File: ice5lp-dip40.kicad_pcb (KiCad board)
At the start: 2 copper layers, 17.8 x 50.8 mm, 43 parts, among them J1 Conn_02x04_Odd_Even, J2 Conn_01x20, J3 Conn_01x20, J4 USB_B_Micro, SW1 SW_Push, SW2 SW_Push, U1 AT25D011-SSHF, U2 MIC5355-S4YMME, U3 ICE5LP4K-SG48, X1 ECS-2520MV-500-BN-TR

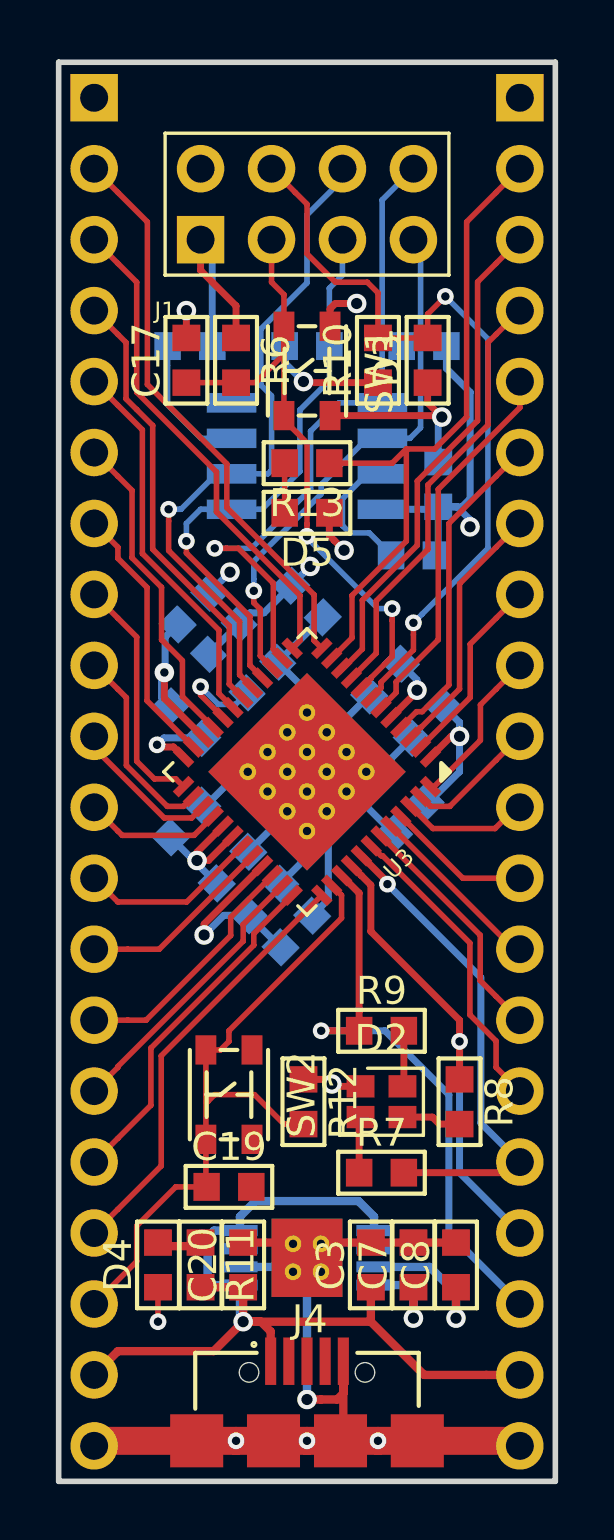
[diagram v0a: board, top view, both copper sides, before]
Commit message: Fix some DRC errors on PCB
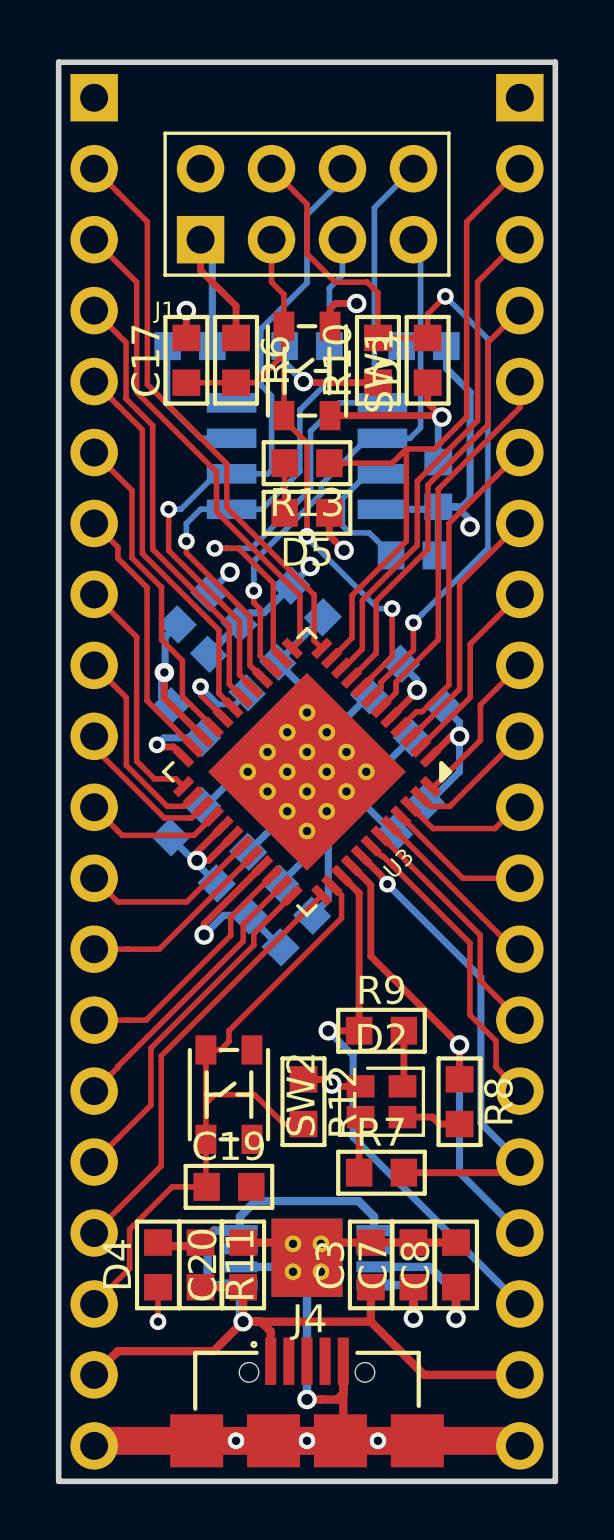
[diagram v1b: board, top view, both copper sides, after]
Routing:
- net RGB_B: track 21.3 -> 19.6 mm
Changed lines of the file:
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@@
   (segment (start 191.262 73.66) (end 191.262 74.295) (width 0.2) (layer B.Cu) (net 6))
   (segment (start 191.77 73.152) (end 191.262 73.66) (width 0.2) (layer B.Cu) (net 6))
-  (segment (start 198.269999 68.781999) (end 198.269999 62.080001) (width 0.2) (layer B.Cu) (net 7))
-  (segment (start 198.28 69.342) (end 198.28 68.792) (width 0.2) (layer B.Cu) (net 7) (status 10))
-  (segment (start 198.269999 62.080001) (end 199.39 60.96) (width 0.2) (layer B.Cu) (net 7) (status 20))
-  (segment (start 198.28 68.792) (end 198.269999 68.781999) (width 0.2) (layer B.Cu) (net 7))
   (via (at 192.278 74.549) (size 0.6) (drill 0.3) (layers F.Cu B.Cu) (net 7))
   (segment (start 195.707 70.358) (end 195.707 72.433264) (width 0.2) (layer B.Cu) (net 7))
@@
   (segment (start 194.372002 75.799398) (end 193.121602 74.549) (width 0.2) (layer F.Cu) (net 7))
   (segment (start 192.702264 74.549) (end 192.278 74.549) (width 0.2) (layer F.Cu) (net 7))
+  (segment (start 197.993 62.357) (end 199.39 60.96) (width 0.2) (layer B.Cu) (net 7))
+  (segment (start 197.993 68.505) (end 197.993 62.357) (width 0.2) (layer B.Cu) (net 7))
+  (segment (start 198.28 69.342) (end 198.28 68.792) (width 0.2) (layer B.Cu) (net 7))
+  (segment (start 198.28 68.792) (end 197.993 68.505) (width 0.2) (layer B.Cu) (net 7))
   (segment (start 190.589 68.01) (end 190.589 67.31) (width 0.2) (layer B.Cu) (net 8))
   (segment (start 190.589 69.411) (end 190.589 68.01) (width 0.2) (layer B.Cu) (net 8))
@@
   (segment (start 191.961 94.107) (end 191.961 94.361) (width 0.2) (layer F.Cu) (net 46))
   (segment (start 191.961 94.361) (end 191.961 95.707) (width 0.2) (layer F.Cu) (net 46) (status 20))
-  (segment (start 190.881 97.409) (end 191.986 97.409) (width 0.2) (layer F.Cu) (net 46) (status 20))
-  (segment (start 189.484 98.806) (end 190.881 97.409) (width 0.2) (layer F.Cu) (net 46))
-  (segment (start 187.96 101.6) (end 189.484 100.076) (width 0.2) (layer F.Cu) (net 46) (status 10))
-  (segment (start 189.484 100.076) (end 189.484 98.806) (width 0.2) (layer F.Cu) (net 46))
   (segment (start 193.699 94.107) (end 192.278 94.107) (width 0.2) (layer F.Cu) (net 46))
   (segment (start 195.453 95.161) (end 194.753 95.161) (width 0.2) (layer F.Cu) (net 46) (status 10))
@@
   (segment (start 191.961 92.507) (end 192.481 92.507) (width 0.2) (layer F.Cu) (net 46))
   (segment (start 192.481 92.507) (end 192.786 92.202) (width 0.2) (layer F.Cu) (net 46))
+  (segment (start 190.754 97.409) (end 191.986 97.409) (width 0.2) (layer F.Cu) (net 46))
+  (segment (start 189.23 98.933) (end 190.754 97.409) (width 0.2) (layer F.Cu) (net 46))
+  (segment (start 187.96 101.6) (end 189.23 100.33) (width 0.2) (layer F.Cu) (net 46))
+  (segment (start 189.23 100.33) (end 189.23 98.933) (width 0.2) (layer F.Cu) (net 46))
   (segment (start 197.447 91.121) (end 197.447 91.821) (width 0.25) (layer F.Cu) (net 47) (status 20))
   (segment (start 197.474009 91.093991) (end 197.447 91.121) (width 0.2) (layer F.Cu) (net 47))
-  (via (at 196.088 91.821) (size 0.6) (drill 0.3) (layers F.Cu B.Cu) (net 47))
-  (segment (start 197.447 91.821) (end 196.088 91.821) (width 0.25) (layer F.Cu) (net 47) (status 10))
-  (segment (start 200.66 94.107) (end 200.66 99.06) (width 0.25) (layer B.Cu) (net 47))
-  (segment (start 200.66 99.06) (end 203.2 101.6) (width 0.25) (layer B.Cu) (net 47) (status 20))
-  (segment (start 196.088 91.821) (end 198.374 91.821) (width 0.25) (layer B.Cu) (net 47))
-  (segment (start 198.374 91.821) (end 200.66 94.107) (width 0.25) (layer B.Cu) (net 47))
   (segment (start 196.817437 86.262311) (end 197.445989 86.890863) (width 0.25) (layer F.Cu) (net 47))
   (segment (start 197.445989 86.890863) (end 197.445989 91.065971) (width 0.25) (layer F.Cu) (net 47))
   (segment (start 197.445989 91.065971) (end 197.474009 91.093991) (width 0.25) (layer F.Cu) (net 47))
-  (segment (start 201.041 93.561) (end 201.041 92.202) (width 0.25) (layer F.Cu) (net 48) (status 10))
-  (via (at 201.041 92.202) (size 0.6) (drill 0.3) (layers F.Cu B.Cu) (net 48))
-  (segment (start 201.041 96.901) (end 203.2 99.06) (width 0.25) (layer B.Cu) (net 48) (status 20))
-  (segment (start 201.041 92.202) (end 201.041 96.901) (width 0.25) (layer B.Cu) (net 48))
-  (segment (start 197.524543 86.26231) (end 197.17099 85.908757) (width 0.25) (layer F.Cu) (net 48))
-  (segment (start 197.866 86.603767) (end 197.524543 86.26231) (width 0.25) (layer F.Cu) (net 48))
-  (segment (start 201.041 91.44) (end 197.866 88.265) (width 0.25) (layer F.Cu) (net 48))
-  (segment (start 197.866 88.265) (end 197.866 86.603767) (width 0.25) (layer F.Cu) (net 48))
-  (segment (start 201.041 92.202) (end 201.041 91.44) (width 0.25) (layer F.Cu) (net 48))
+  (via (at 196.342016 91.821) (size 0.7) (drill 0.4) (layers F.Cu B.Cu) (net 47))
+  (segment (start 197.447 91.821) (end 196.342016 91.821) (width 0.25) (layer F.Cu) (net 47))
+  (segment (start 203.2 101.6) (end 197.231 95.631) (width 0.25) (layer B.Cu) (net 47))
+  (segment (start 197.231 95.631) (end 197.231 92.709984) (width 0.25) (layer B.Cu) (net 47))
+  (segment (start 196.642015 92.120999) (end 196.342016 91.821) (width 0.25) (layer B.Cu) (net 47))
+  (segment (start 197.231 92.709984) (end 196.642015 92.120999) (width 0.25) (layer B.Cu) (net 47))
+  (via (at 201.041 92.32901) (size 0.7) (drill 0.4) (layers F.Cu B.Cu) (net 48))
+  (segment (start 201.041 93.561) (end 201.041 92.32901) (width 0.25) (layer F.Cu) (net 48))
+  (segment (start 200.691001 91.979011) (end 201.041 92.32901) (width 0.25) (layer F.Cu) (net 48))
+  (segment (start 201.041 96.901) (end 201.041 92.823984) (width 0.25) (layer B.Cu) (net 48))
+  (segment (start 201.041 92.823984) (end 201.041 92.32901) (width 0.25) (layer B.Cu) (net 48))
+  (segment (start 203.2 99.06) (end 201.041 96.901) (width 0.25) (layer B.Cu) (net 48))
+  (segment (start 197.866 89.15401) (end 200.691001 91.979011) (width 0.25) (layer F.Cu) (net 48))
+  (segment (start 197.866 86.603767) (end 197.866 89.15401) (width 0.25) (layer F.Cu) (net 48))
+  (segment (start 197.17099 85.908757) (end 197.866 86.603767) (width 0.25) (layer F.Cu) (net 48))
   (segment (start 202.819 96.901) (end 203.2 96.52) (width 0.2) (layer F.Cu) (net 49) (status 30))
   (segment (start 199.047 96.901) (end 202.819 96.901) (width 0.25) (layer F.Cu) (net 49) (status 30))

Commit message: Add 2 inner layers and route power
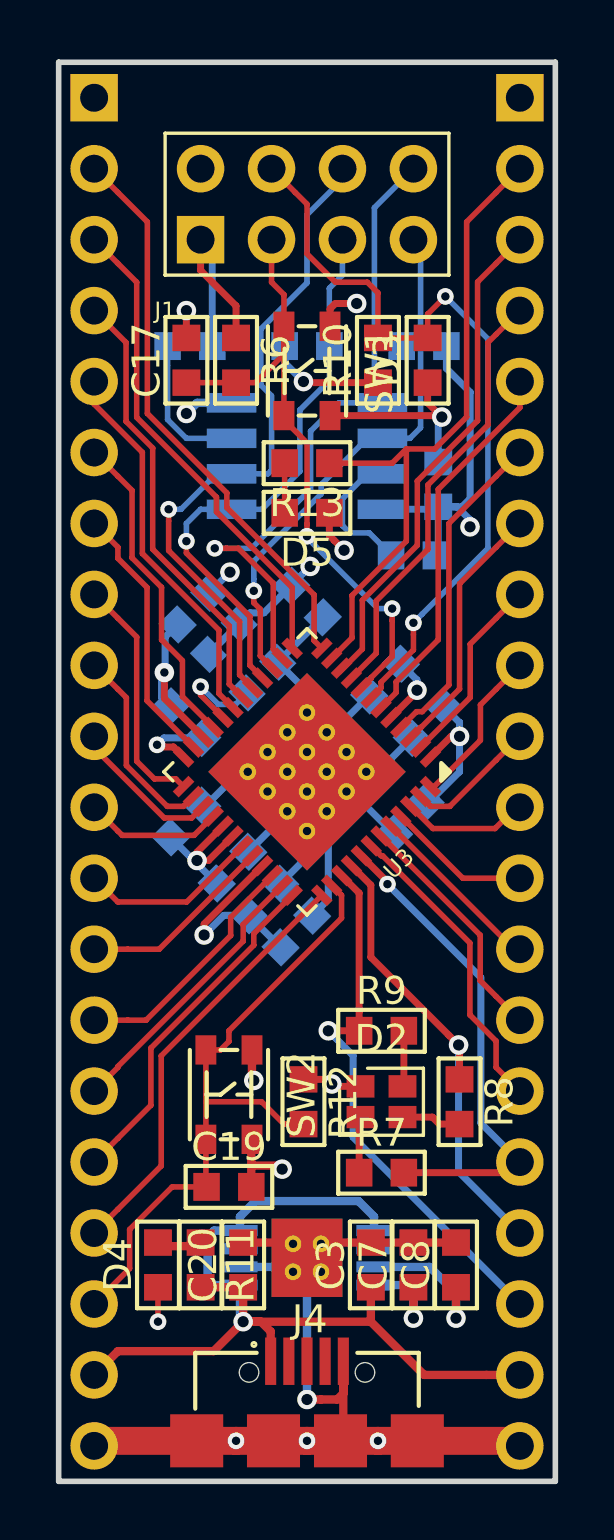
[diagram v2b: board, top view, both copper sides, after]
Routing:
- net VCC_IO: track 53.9 -> 177.6 mm
- net VCC_CORE: track 13.5 -> 46.8 mm
- net GND: track 83.7 -> 89.5 mm, vias 10 -> 13
- added copper zone on In2.GND.Cu, net GND
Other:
- copper layers 2 -> 4

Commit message: Increase power tracks width
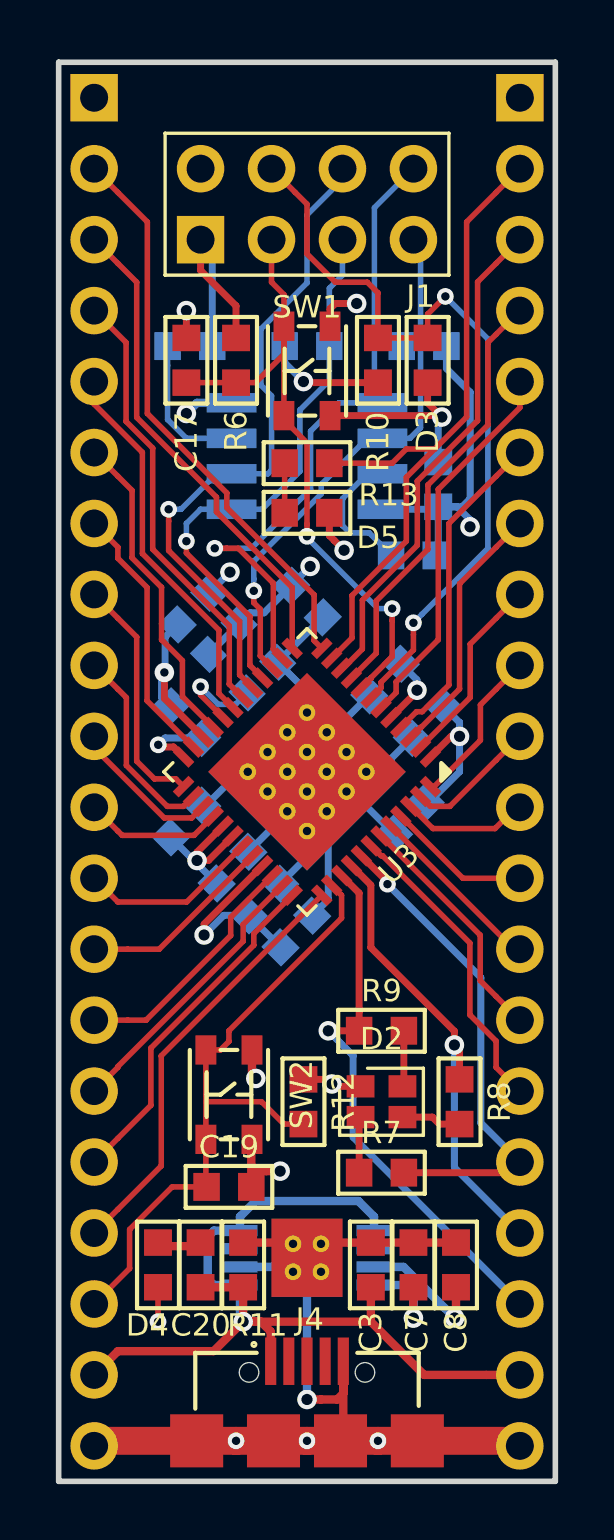
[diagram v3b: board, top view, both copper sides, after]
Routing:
- net VCC_IO: track 177.6 -> 178.8 mm
- net VCC_CORE: track 46.8 -> 46.2 mm

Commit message: Beautify Silk and Fab layers
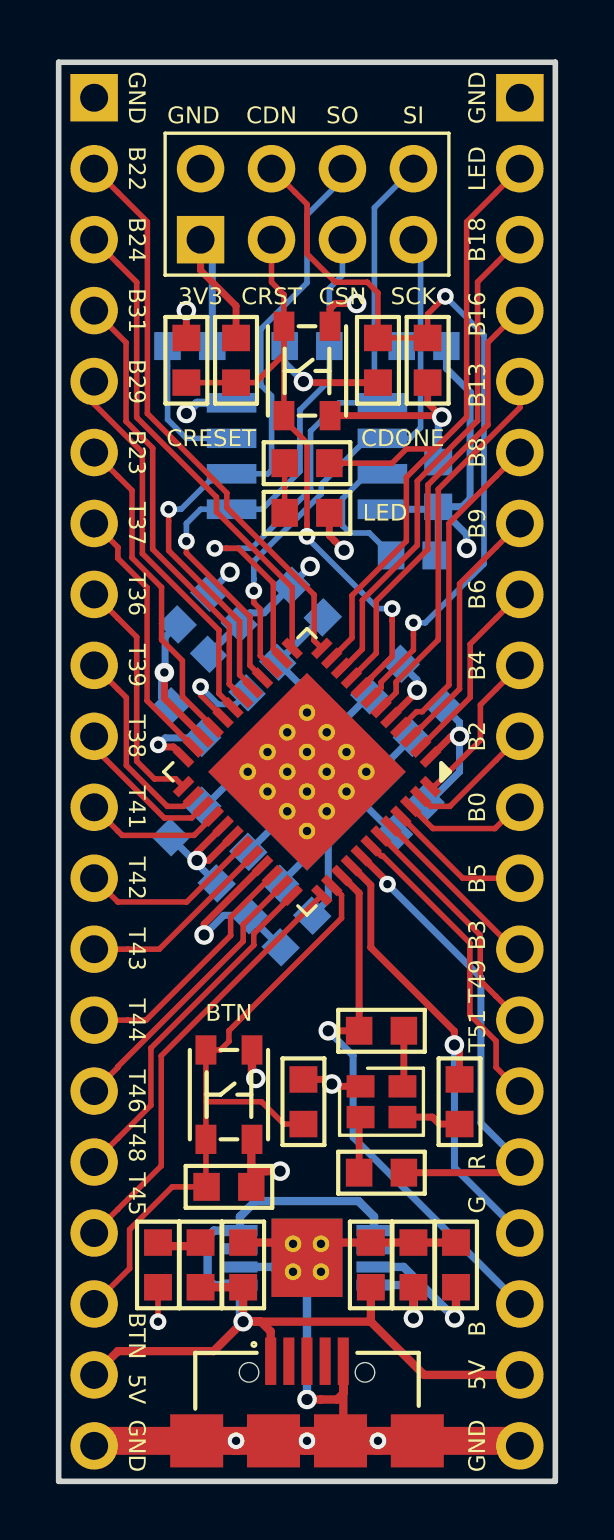
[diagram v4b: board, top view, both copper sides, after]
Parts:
- renumbered R2 to eR2
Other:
- board text added: "3V3"
- board text added: "5V"
- board text added: "B"
- board text added: "B0"
- board text added: "B13"
- board text added: "B16"
- board text added: "B18"
- board text added: "B2"
- board text added: "B22"
- board text added: "B23"
- board text added: "B24"
- board text added: "B29"
- board text added: "B3"
- board text added: "B31"
- board text added: "B4"
- board text added: "B5"
- board text added: "B6"
- board text added: "B8"
- board text added: "B9"
- board text added: "BTN"
- board text added: "CDN"
- board text added: "CDONE"
- board text added: "CRESET"
- board text added: "CRST"
- board text added: "CSN"
- board text added: "G"
- board text added: "GND"
- board text added: "LED"
- board text added: "R"
- board text added: "SCK"
- board text added: "SI"
- board text added: "SO"
- board text added: "T36"
- board text added: "T37"
- board text added: "T38"
- board text added: "T39"
- board text added: "T41"
- board text added: "T42"
- board text added: "T43"
- board text added: "T44"
- board text added: "T45"
- board text added: "T46"
- board text added: "T48"
- board text added: "T49"
- board text added: "T51"

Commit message: Add logo and final Silk edits
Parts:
- added G***: LOGO, esynr3z_Symbol:esynr3z_logo_4.5x8.4mm_Silk, B.Cu at (199.0, 93.2)
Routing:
- net IOT_42B: track 6.51 -> 5.80 mm
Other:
- board text added: "DIP40"
- board text added: "ICE5LP"
- board text added: "esynr3z"

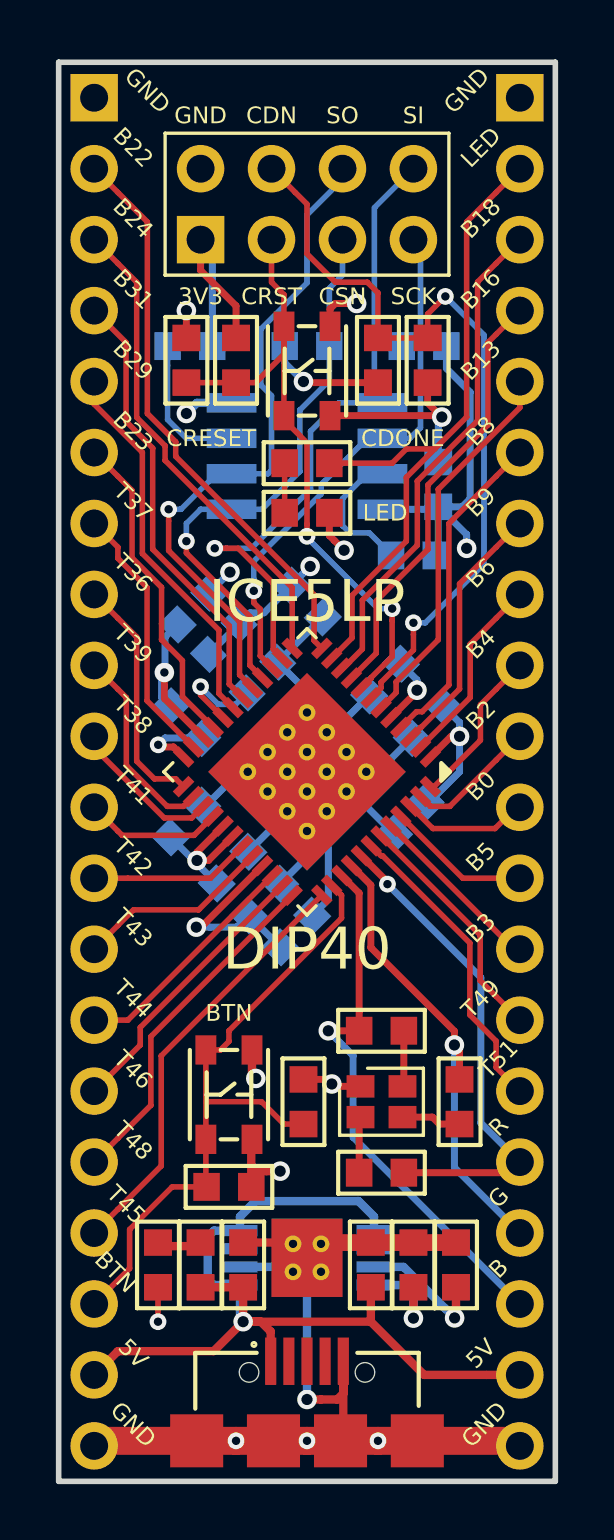
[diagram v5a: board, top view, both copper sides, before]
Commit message: Some minor pcb fixes
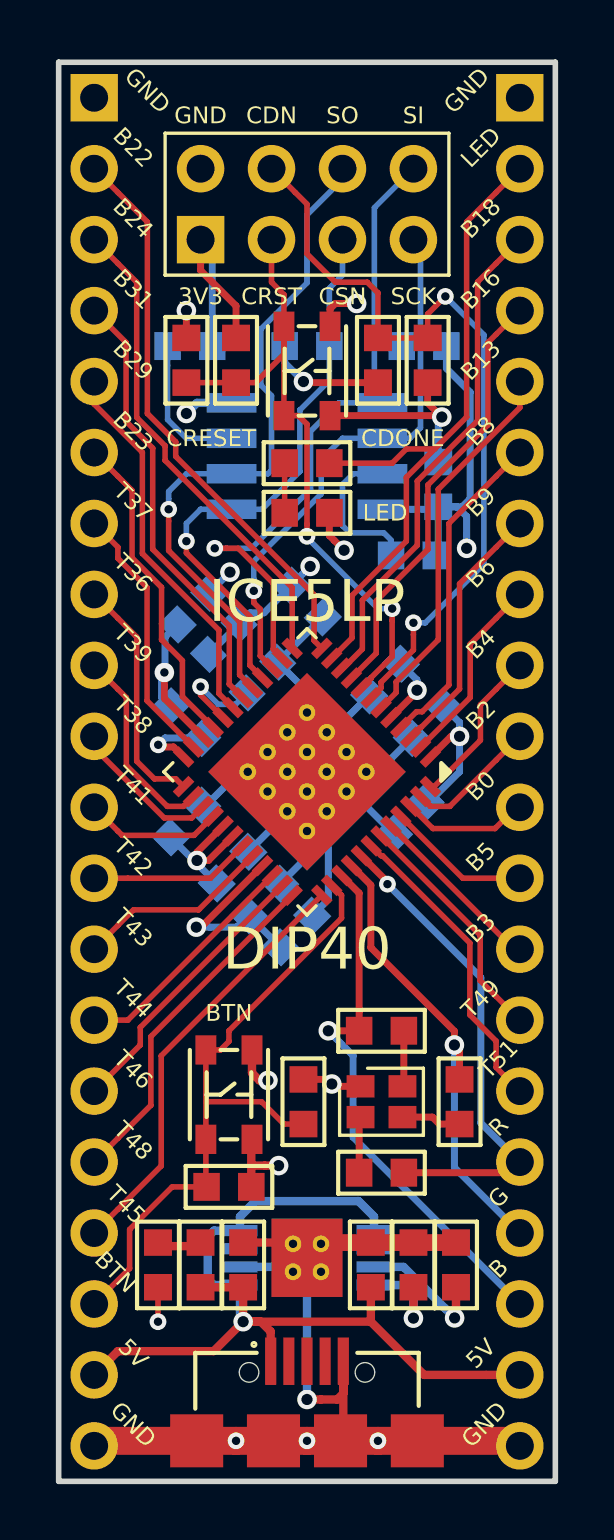
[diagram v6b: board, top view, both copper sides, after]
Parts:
- renumbered eR2 to R2
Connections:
- J4 pad 2: (no net) -> Net-(J4-Pad2)
- J4 pad 3: (no net) -> Net-(J4-Pad3)
- J4 pad 4: (no net) -> Net-(J4-Pad4)
- U2 pad 3: (no net) -> Net-(U2-Pad3)
- U2 pad 6: (no net) -> Net-(U2-Pad6)
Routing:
- net Net-(R4-Pad2): track 4.96 -> 5.56 mm
- net ICE_SCK: track 19.8 -> 20.3 mm
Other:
- board text added: "ice5lp-dip40 v1.0"
